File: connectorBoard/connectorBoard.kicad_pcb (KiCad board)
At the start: 2 copper layers, 6 parts, among them J1 Conn_01x08_Female

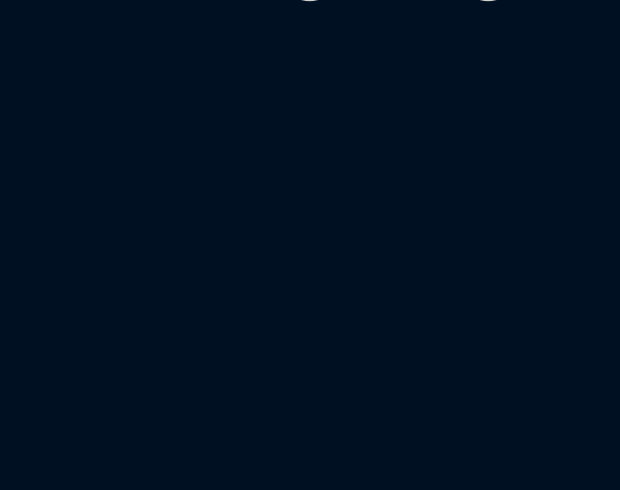
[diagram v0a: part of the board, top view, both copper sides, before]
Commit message: added missing connector
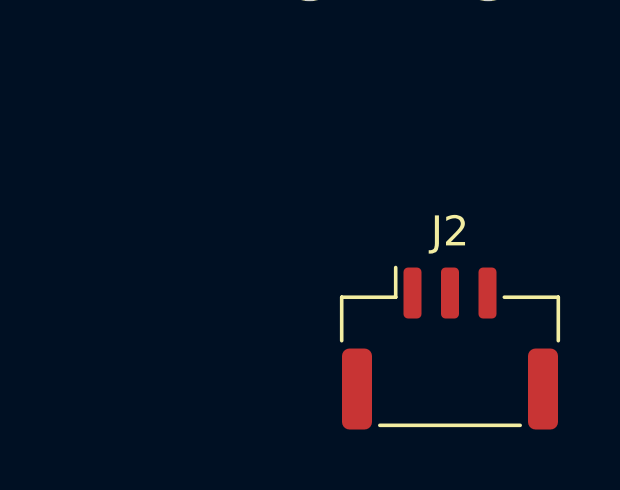
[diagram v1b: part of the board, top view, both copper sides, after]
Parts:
- added J2: Conn_01x03_Male, Connector_JST:JST_GH_SM03B-GHS-TB_1x03-1MP_P1.25mm_Horizontal, F.Cu at (156.2, 105.4)
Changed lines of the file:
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@@
   (net 7 "unconnected-(J1-Pad4)")
   (net 8 "unconnected-(J1-Pad5)")
+  (footprint "Connector_JST:JST_GH_SM03B-GHS-TB_1x03-1MP_P1.25mm_Horizontal" (layer "F.Cu")
+    (at 156.21 105.41)
+    (descr "JST GH series connector, SM03B-GHS-TB (http://www.jst-mfg.com/product/pdf/eng/eGH.pdf), generated with kicad-footprint-generator")
+    (tags "connector JST GH top entry")
+    (property "Sheetfile" "connectorBoard.kicad_sch")
+    (property "Sheetname" "")
+    (attr smd)
+    (fp_text reference "J2" (at 0 -3.9) (layer "F.SilkS")
+      (effects (font (size 1 1) (thickness 0.15)))
+    )
+    (fp_text value "Conn_01x03_Male" (at 0 3.9) (layer "F.Fab")
+      (effects (font (size 1 1) (thickness 0.15)))
+    )
+    (fp_text user "${REFERENCE}" (at 0 0) (layer "F.Fab")
+      (effects (font (size 1 1) (thickness 0.15)))
+    )
+    (fp_line (start -3.61 -1.71) (end -1.81 -1.71) (layer "F.SilkS") (width 0.12))
+    (fp_line (start 3.61 -1.71) (end 1.81 -1.71) (layer "F.SilkS") (width 0.12))
+    (fp_line (start -1.81 -1.71) (end -1.81 -2.7) (layer "F.SilkS") (width 0.12))
+    (fp_line (start -2.34 2.56) (end 2.34 2.56) (layer "F.SilkS") (width 0.12))
+    (fp_line (start 3.61 -0.26) (end 3.61 -1.71) (layer "F.SilkS") (width 0.12))
+    (fp_line (start -3.61 -0.26) (end -3.61 -1.71) (layer "F.SilkS") (width 0.12))
+    (fp_line (start -4.1 3.2) (end 4.1 3.2) (layer "F.CrtYd") (width 0.05))
+    (fp_line (start 4.1 -3.2) (end -4.1 -3.2) (layer "F.CrtYd") (width 0.05))
+    (fp_line (start 4.1 3.2) (end 4.1 -3.2) (layer "F.CrtYd") (width 0.05))
+    (fp_line (start -4.1 -3.2) (end -4.1 3.2) (layer "F.CrtYd") (width 0.05))
+    (fp_line (start -1.75 -1.6) (end -1.25 -0.892893) (layer "F.Fab") (width 0.1))
+    (fp_line (start -3.5 2.45) (end 3.5 2.45) (layer "F.Fab") (width 0.1))
+    (fp_line (start -3.5 -1.6) (end -3.5 2.45) (layer "F.Fab") (width 0.1))
+    (fp_line (start -1.25 -0.892893) (end -0.75 -1.6) (layer "F.Fab") (width 0.1))
+    (fp_line (start -3.5 -1.6) (end 3.5 -1.6) (layer "F.Fab") (width 0.1))
+    (fp_line (start 3.5 -1.6) (end 3.5 2.45) (layer "F.Fab") (width 0.1))
+    (pad "1" smd roundrect (at -1.25 -1.85) (size 0.6 1.7) (layers "F.Cu" "F.Paste" "F.Mask") (roundrect_rratio 0.25)
+      (net 1 "VCC") (pinfunction "Pin_1") (pintype "passive"))
+    (pad "2" smd roundrect (at 0 -1.85) (size 0.6 1.7) (layers "F.Cu" "F.Paste" "F.Mask") (roundrect_rratio 0.25)
+      (net 3 "/C-Data") (pinfunction "Pin_2") (pintype "passive"))
+    (pad "3" smd roundrect (at 1.25 -1.85) (size 0.6 1.7) (layers "F.Cu" "F.Paste" "F.Mask") (roundrect_rratio 0.25)
+      (net 2 "GND") (pinfunction "Pin_3") (pintype "passive"))
+    (pad "MP" smd roundrect (at -3.1 1.35) (size 1 2.7) (layers "F.Cu" "F.Paste" "F.Mask") (roundrect_rratio 0.25))
+    (pad "MP" smd roundrect (at 3.1 1.35) (size 1 2.7) (layers "F.Cu" "F.Paste" "F.Mask") (roundrect_rratio 0.25))
+    (model "${KICAD6_3DMODEL_DIR}/Connector_JST.3dshapes/JST_GH_SM03B-GHS-TB_1x03-1MP_P1.25mm_Horizontal.wrl"
+      (offset (xyz 0 0 0))
+      (scale (xyz 1 1 1))
+      (rotate (xyz 0 0 0))
+    )
+  )
   (footprint "Diode_SMD:D_SOD-323F" (layer "F.Cu")
     (at 137.16 105.41)

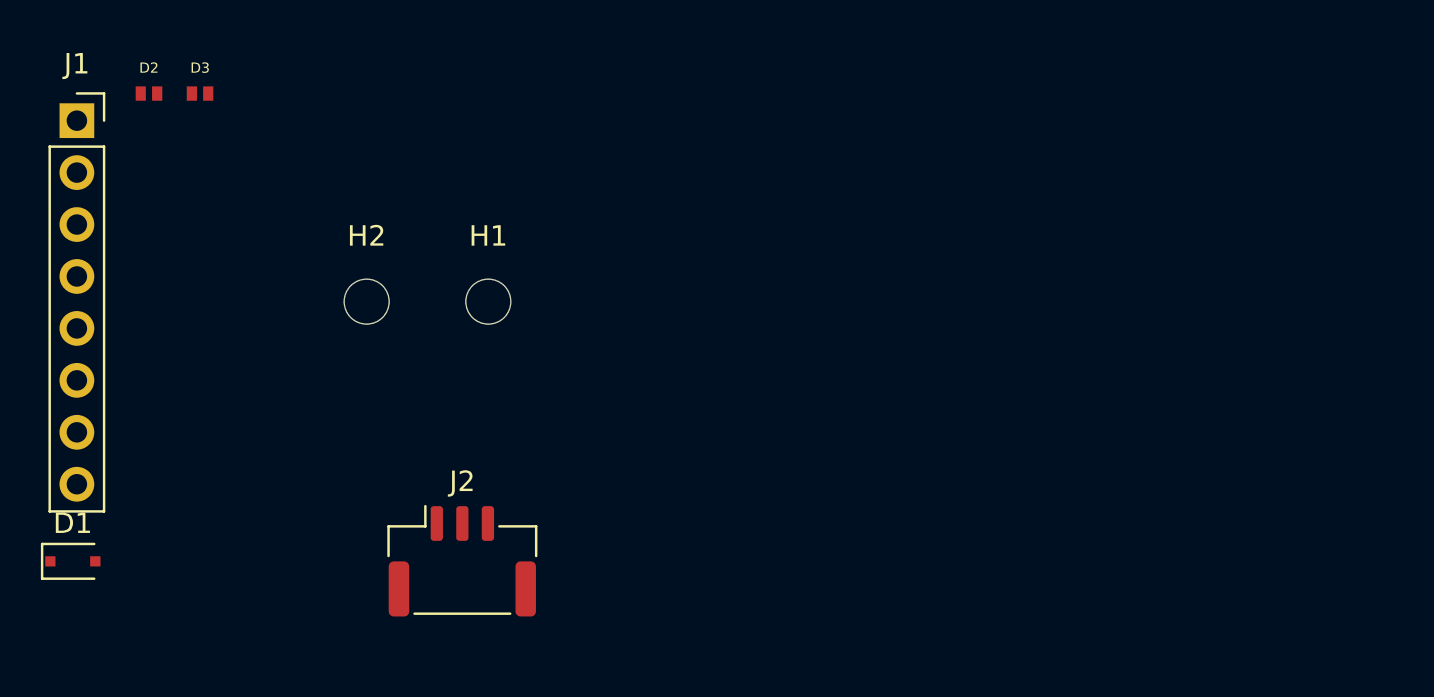
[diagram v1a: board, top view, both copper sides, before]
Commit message: basic connector pcb design
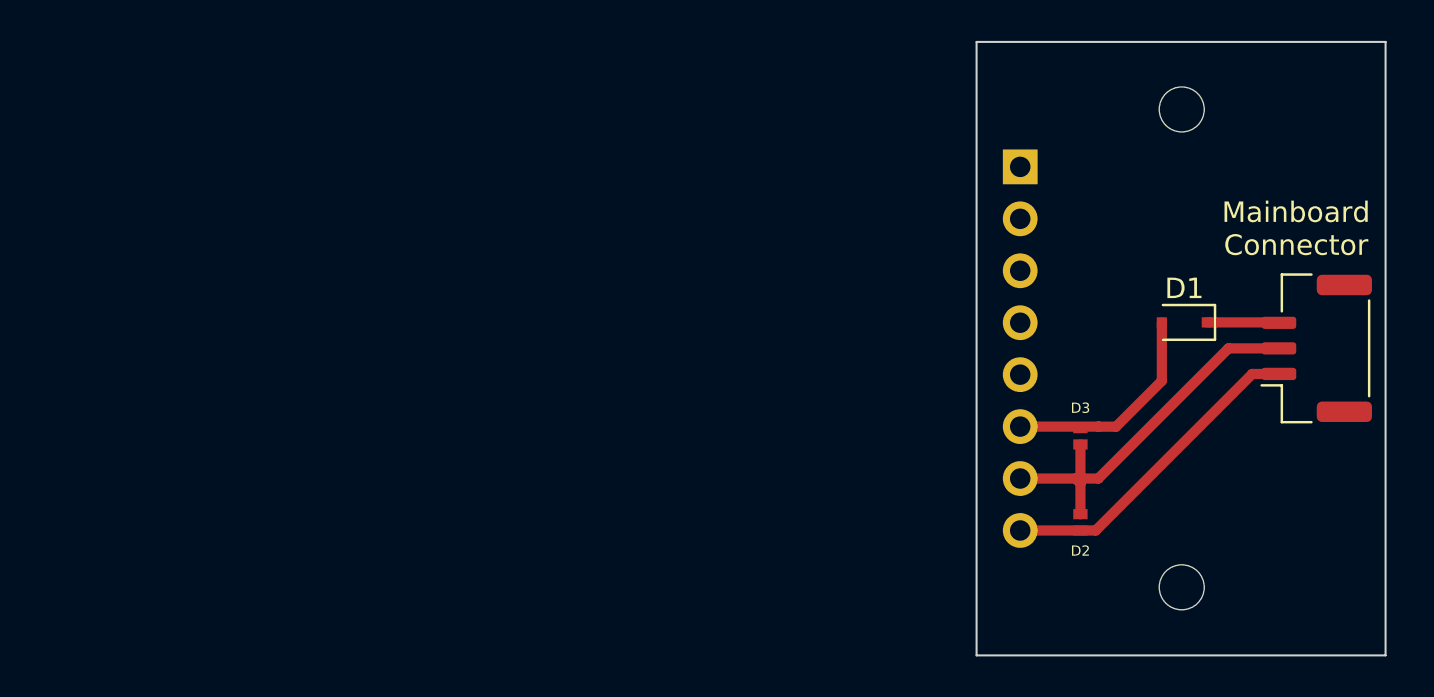
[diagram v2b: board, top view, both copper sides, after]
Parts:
- J1: moved to B.Cu
- moved D1 55.6 mm to (191.5, 93.7), turned to 180 degrees
- moved D2 50.1 mm to (186.4, 103.5), turned to -90 degrees
- moved D3 46.2 mm to (186.4, 99.3), turned to -90 degrees
- moved J1 46.2 mm to (183.5, 86.1), turned to 180 degrees
- moved J2 43.1 mm to (198.0, 95.0), turned to 90 degrees
- moved H2 41.0 mm to (191.4, 83.3)
- moved H1 36.7 mm to (191.4, 106.7)
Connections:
- D1 pad 2: VCC -> Net-(D1-Pad2)
- D3 pad 1: VCC -> Net-(D1-Pad2)
- J1 pad 6: VCC -> Net-(D1-Pad2)
- J2 pad 1: VCC -> /C-Data
- J2 pad 2: /C-Data -> GND
- J2 pad 3: GND -> VCC
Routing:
- net GND: track 0.00 -> 19.0 mm
- net /C-Data: track 0.00 -> 15.8 mm
- net Net-(D1-Pad2): track 0.00 -> 10.7 mm
- net VCC: track 0.00 -> 3.54 mm
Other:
- board outline added: 20 x 30 mm
- board text added: "Controller Connector"
- board text added: "Mainboard Connector"

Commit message: updates for the connector board
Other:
- outline, holes or cut-outs redrawn
- board text added: "+"
- board text added: "Connectorboard v0.9"
- board text added: "JLCJLCJLCJLC"
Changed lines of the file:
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@@
     )
   )
-  (gr_line (start 201.356 110.01) (end 181.356 110.01) (layer "Edge.Cuts") (width 0.1))
-  (gr_line (start 181.356 110.01) (end 181.356 80.01) (layer "Edge.Cuts") (width 0.1))
-  (gr_line (start 201.356 80.01) (end 201.356 110.01) (layer "Edge.Cuts") (width 0.1))
-  (gr_line (start 181.356 80.01) (end 201.356 80.01) (layer "Edge.Cuts") (width 0.1))
+  (gr_circle (center 194.6 96.275) (end 194.736 96.284) (layer "F.SilkS") (width 0.15) (fill none))
+  (gr_line (start 200.594 110.01) (end 182.118 110.01) (layer "Edge.Cuts") (width 0.1))
+  (gr_line (start 181.356 109.248) (end 181.356 80.772) (layer "Edge.Cuts") (width 0.1))
+  (gr_arc (start 182.118 110.01) (mid 181.579185 109.786815) (end 181.356 109.248) (layer "Edge.Cuts") (width 0.1))
+  (gr_arc (start 181.356 80.772) (mid 181.579185 80.233185) (end 182.118 80.01) (layer "Edge.Cuts") (width 0.1))
+  (gr_line (start 201.356 80.772) (end 201.356 109.248) (layer "Edge.Cuts") (width 0.1))
+  (gr_arc (start 201.356 109.248) (mid 201.132815 109.786815) (end 200.594 110.01) (layer "Edge.Cuts") (width 0.1))
+  (gr_arc (start 200.594 80.01) (mid 201.132815 80.233185) (end 201.356 80.772) (layer "Edge.Cuts") (width 0.1))
+  (gr_line (start 182.118 80.01) (end 200.594 80.01) (layer "Edge.Cuts") (width 0.1))
   (gr_line (start 201.356 80) (end 201.356 110) (layer "User.1") (width 0.15))
   (gr_line (start 181.356 80) (end 181.356 110) (layer "User.1") (width 0.15))
   (gr_line (start 181.356 110) (end 201.356 110) (layer "User.1") (width 0.15))
   (gr_line (start 181.356 80) (end 201.356 80) (layer "User.1") (width 0.15))
+  (gr_text "Connectorboard\nv0.9" (at 199.136 94.996 90) (layer "B.SilkS")
+    (effects (font (size 1 1) (thickness 0.15)) (justify mirror))
+  )
   (gr_text "Controller Connector" (at 186.436 94.742 90) (layer "B.SilkS")
     (effects (font (size 1 1) (thickness 0.15)) (justify mirror))
   )
+  (gr_text "+" (at 187.075 100.175) (layer "F.SilkS")
+    (effects (font (size 0.6 0.6) (thickness 0.15)))
+  )
+  (gr_text "JLCJLCJLCJLC" (at 199.898 104.648 90) (layer "F.SilkS")
+    (effects (font (size 0.8 0.8) (thickness 0.15)))
+  )
+  (gr_text "+" (at 189.475 93.675) (layer "F.SilkS")
+    (effects (font (size 0.8 0.8) (thickness 0.15)))
+  )
+  (gr_text "+" (at 187.075 102.575) (layer "F.SilkS")
+    (effects (font (size 0.6 0.6) (thickness 0.15)))
+  )
   (gr_text "Mainboard\nConnector" (at 196.977 89.154) (layer "F.SilkS")

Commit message: cleanup
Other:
- board text added: "Connectorboard v1.0"
- board text removed: "Connectorboard v0.9"
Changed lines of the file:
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@@
   )
   (paper "A4")
+  (title_block
+    (title "Connector Board")
+    (date "2023-02-14")
+    (rev "1.0")
+    (company "Fabian Kuffer")
+  )
   (layers
     (0 "F.Cu" signal)
@@
   (gr_line (start 181.356 110) (end 201.356 110) (layer "User.1") (width 0.15))
   (gr_line (start 181.356 80) (end 201.356 80) (layer "User.1") (width 0.15))
-  (gr_text "Connectorboard\nv0.9" (at 199.136 94.996 90) (layer "B.SilkS")
+  (gr_text "Connectorboard\nv1.0" (at 199.136 94.996 90) (layer "B.SilkS")
     (effects (font (size 1 1) (thickness 0.15)) (justify mirror))
   )
